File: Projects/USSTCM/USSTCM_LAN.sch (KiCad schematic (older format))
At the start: 64 parts, among them IC3 RASPI_LAN9514, IC5 FSUSB42MSOP10, Q3 DMG1012T, Q4 DMG1012T, Q6 CTS_32X25_SMD

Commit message: Refactoring Compute Module project for 2017 USST KiCad library format
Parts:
- removed C14: 100n, USSTCM:RCL_C0603, symbol RCL_C-EUC0603
- removed D2, D3, D4, D6: BAV99, USSTCM:DIODE_SOT23, symbol DIODE_BAV199
- removed D5: BAT54, USSTCM:DIODE_SOT23, symbol DIODE_BAT54
- removed HDMI55: HDMI, USSTCM:RASPI_HDMI, symbol RASPI_HDMI
- removed Q4: DMG1012T, USSTCM:TRANSISTOR-FET_SC75_INFINEON, symbol TRANSISTOR-FET_BSA223SP
- removed R10: 100k, USSTCM:RCL_R0603, symbol RCL_R-EU_R0603
- removed R11, R12: 1k8, USSTCM:RCL_R0603, symbol RCL_R-EU_R0603
- removed USB1: MICRO_USB, USSTCM:MASTER_CLOCK_MICRO_USB, symbol MASTER_CLOCK_MICRO_USB
- added USB?: USB-TYPA, USB-A-F-PTH, symbol USB-TYPA
- C11, C12, C41, C42: symbol RCL_C-EUC0805 -> C
- C13, C21, C22, C23, C24, C26, C27, C28, C29, C30, C31, C32, C33, C34, C35, C36, C37, C38, C39, C4, C40, C43, C44, C45, C7: symbol RCL_C-EUC0603 -> C
- ETHERNET55: symbol HANRUN_HR911105A -> HANRUN-HR911105A
- FB1, FB2: symbol RASPI_FERRITE_BEAD -> FERRITE_BEAD
- IC3: symbol RASPI_LAN9514 -> LAN9514
- IC5: symbol RASPI_FSUSB42MSOP10 -> FSUSB42MSOP10
- Q3: symbol TRANSISTOR-FET_BSA223SP -> Q_PMOS_GDS
- Q6: symbol RASPI_CTS_32X25_SMD -> Crystal_Small
- R13, R20, R25, R26, R27, R28, R29, R30, R31, R32, R33, R37, R7, R8, R9: symbol RCL_R-EU_R0603 -> R
- USB55: symbol RASPI_USB2 -> USB-TYPA
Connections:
- net +5V: now also USB55.VBUS; no longer USB55.1-1 (1), USB55.2-1 (1)
- net 3V3: now also R20.1, R32.1, R37.2, R8.1; no longer R20.2, R25.1, R26.1, R32.2, R37.1, R8.2
- net GND: now also IC3.65 (GND), Q3.2 (D), R33.1, R7.2, R9.2, USB55.GND, USB?.GND; no longer IC3.EXP (GND), Q3.3 (S), R33.2, R7.1, R9.1, USB55.1-4 (4), USB55.2-4 (4)
- net GPIO6: now also R37.1; no longer R37.2
- net VUSB_BOOT: now also R7.1, USB?.VBUS; no longer R7.2
- net XI: now also R13.1; no longer R13.2
- net XO: now also Q6.2, R13.2; no longer Q6.3 (X2), R13.1
- net 3V3A: no longer names the net of C32.2, C33.2, C35.2, C36.2, C37.2, C38.2, FB1.1 (P$1), IC3.10 (VDD33A), IC3.49 (VDD33A), IC3.5 (VDD33A), IC3.51 (VDD33A), IC3.54 (VDD33A), IC3.57 (VDD33A), IC3.64 (VDD33A)
- net 3V3A: no longer C34.2, C4.1, C7.1, R27.1, R28.1, R29.1, R30.1, R31.1
- net N$11: no longer names the net of IC3.63 (USBRBIAS)
- net N$11: now also R9.1; no longer R9.2
- net N$17: no longer names the net of C26.1, ETHERNET55.4, ETHERNET55.5
- net N$17: now also R27.1; no longer R27.2
- removed net N$29: IC5.2 (SEL), Q3.2 (D), R8.1
- net N$40: no longer names the net of C42.2, FB2.2 (P$2), IC3.62 (VDD18USBPLL)
- net N$42: no longer names the net of IC3.41 (AUTOMDXI_EN)
- net N$42: now also R32.2; no longer R32.1
- net N$43: no longer names the net of IC3.50 (EXRES)
- net N$43: now also R33.2; no longer R33.1
- net N$7: no longer names the net of ETHERNET55.12
- net N$7: now also R25.1; no longer R25.2
- net N$8: no longer names the net of ETHERNET55.9
- net N$8: now also R26.1; no longer R26.2
- net N$9: no longer names the net of IC3.28 (NTRST)
- net N$9: now also R20.2; no longer R20.1
- net RX_N: no longer names the net of C24.1, ETHERNET55.6, IC3.53 (RXN), R28.2
- net RX_P: no longer names the net of C23.1, ETHERNET55.3, IC3.52 (RXP)
- net RX_P: now also R29.1; no longer R29.2
- net TX_N: no longer names the net of C22.1, ETHERNET55.2, IC3.56 (TXN)
- net TX_N: now also R30.1; no longer R30.2
- net TX_P: no longer names the net of C21.1, ETHERNET55.1, IC3.55 (TXP)
- net TX_P: now also R31.1; no longer R31.2
- net USBD2_N: no longer names the net of IC3.1 (USBDM2)
- net USBD2_N: no longer USB55.2-2 (2)
- net USBD2_P: no longer names the net of IC3.2 (USBDP2)
- net USBD2_P: no longer USB55.2-3 (3)
- net USBD3_N: no longer names the net of IC3.3 (USBDM3)
- net USBD3_N: now also USB55.D-; no longer USB55.1-2 (2)
- net USBD3_P: no longer names the net of IC3.4 (USBDP3)
- net USBD3_P: now also USB55.D+; no longer USB55.1-3 (3)
- net USBDL_N: no longer names the net of IC3.58 (USBDM0), IC5.8 (HSD2-)
- net USBDL_P: no longer names the net of IC3.59 (USBDP0), IC5.9 (HSD2+)
- net USBDS_N: no longer names the net of IC5.6 (HSD1-)
- net USBDS_N: now also USB?.D-
- net USBDS_P: no longer names the net of IC5.7 (HSD1+)
- net USBDS_P: now also USB?.D+
- new net: IC5.2 (SEL), Q3.3 (S), R8.2
- new net +3V3: C4.1, C7.1, R25.2, R26.2, R27.2, R28.1, R29.2, R30.2, R31.2
- no-connect marks 1 -> 0
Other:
- moved on the sheet: FB1, FB2, IC3, IC5

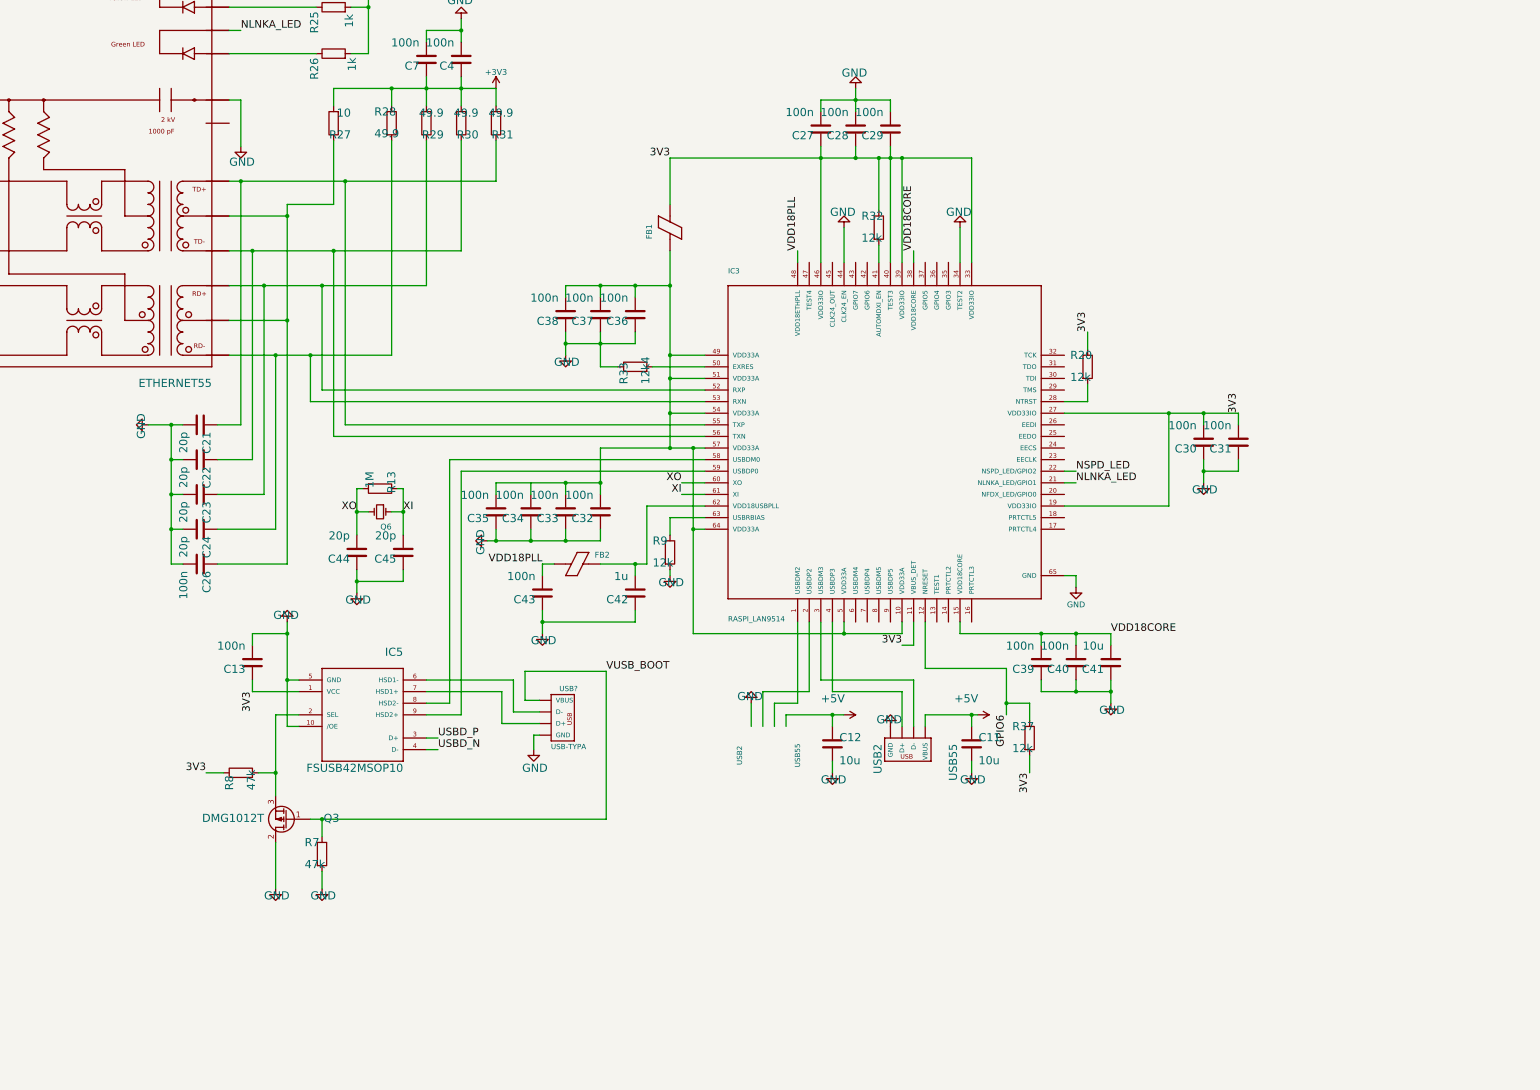
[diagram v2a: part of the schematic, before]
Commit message: More organization of CMIO board
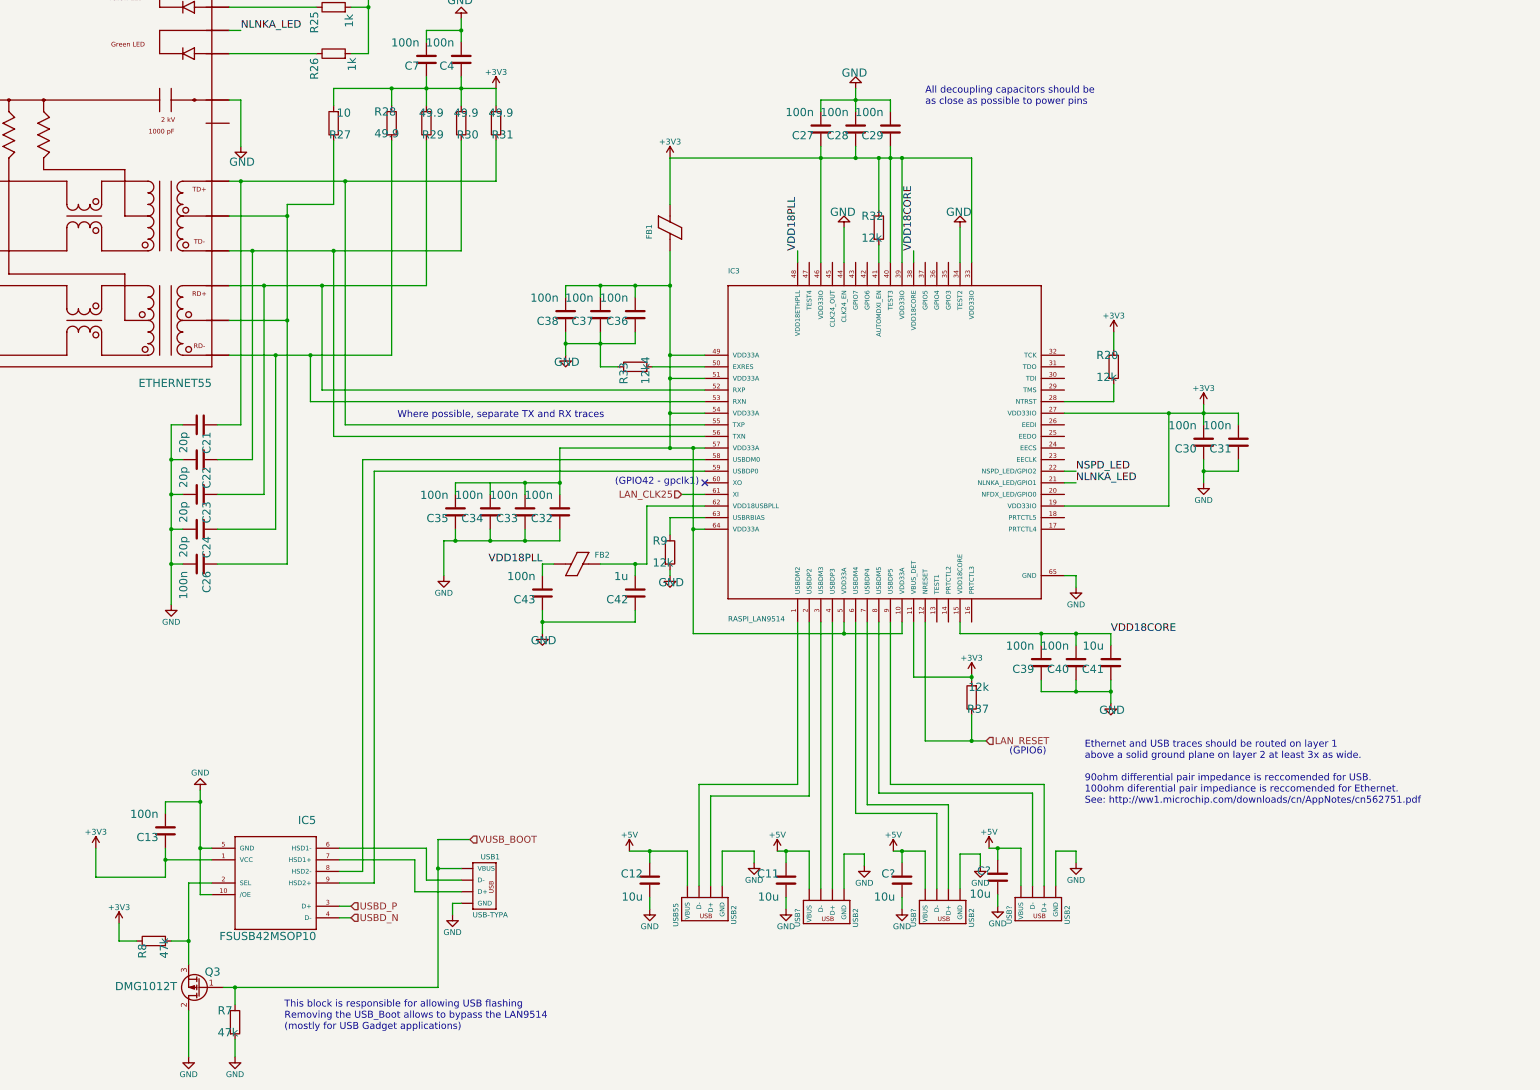
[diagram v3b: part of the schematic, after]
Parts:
- removed C44, C45: 20p, USSTCM:RCL_C0603, symbol C
- removed Q6: CTS_32X25_SMD, USSTCM:RASPI_CTS_32X25, symbol Crystal_Small
- removed R13: 1M, USSTCM:RCL_R0603, symbol R
- added C? (x2): 10u, USSTCM:RCL_C0805, symbol C
- added USB? (x2): USB2, USSTCM:RASPI_USB2, symbol USB-TYPA
- gave numbers to parts that had none: 1
- renumbered USB55 to USB?
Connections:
- net 3V3 is gone; now on net +3V3: C13.1, C27.1, C28.1, C29.1, C30.2, C31.2, FB1.2 (P$2), IC3.11 (VBUS_DET), IC3.19 (VDD33IO), IC3.27 (VDD33IO), IC3.33 (VDD33IO), IC3.39 (VDD33IO), IC3.40 (TEST3), IC3.46 (VDD33IO), IC5.1 (VCC), R20.1, R32.1, R37.2, R8.1
- net +5V: now also USB55.VBUS, C?.1, C?.1, USB?.VBUS, USB?.VBUS
- net GND: now also USB55.GND, C?.2, C?.2, USB?.GND, USB?.GND
- net at IC3.1 (USBDM2): now also USB55.D-
- net at IC3.2 (USBDP2): now also USB55.D+
- net at IC3.6 (USBDM4): now also USB?.D-
- net at IC3.7 (USBDP4): now also USB?.D+
- net at IC3.8 (USBDM5): now also USB?.D-
- net at IC3.9 (USBDP5): now also USB?.D+
- net GPIO6 renamed LAN_RESET
- net XI renamed LAN_CLK25
- net XO: no longer names the net of IC3.60 (XO)
- no-connect marks 0 -> 1
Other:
- note added: "(GPIO42 - gpclk1)"
- note added: "(GPIO6)"
- note added: "All decoupling capacitors should be\nas close as possible to power pins"
- note added: "Ethernet and USB traces should be routed on layer 1\nabove a solid ground plane on layer 2 at least 3x as wide.\n\n90ohm differential pair impedance is reccomended for USB.\n100ohm diferential pair impediance is reccomended for Ethernet.\nSee: http://ww1.microchip.com/downloads/cn/AppNotes/cn562751.pdf"
- note added: "This block is responsible for allowing USB flashing\nRemoving the USB_Boot allows to bypass the LAN9514\n(mostly for USB Gadget applications)"
- note added: "Where possible, separate TX and RX traces"
- moved on the sheet: C11, C12, C13, C32, C33, C34, C35, IC5, Q3, R20, R37, R7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
